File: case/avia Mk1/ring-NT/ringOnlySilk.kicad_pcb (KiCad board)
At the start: 2 copper layers, 44 x 43.6 mm, 1 part

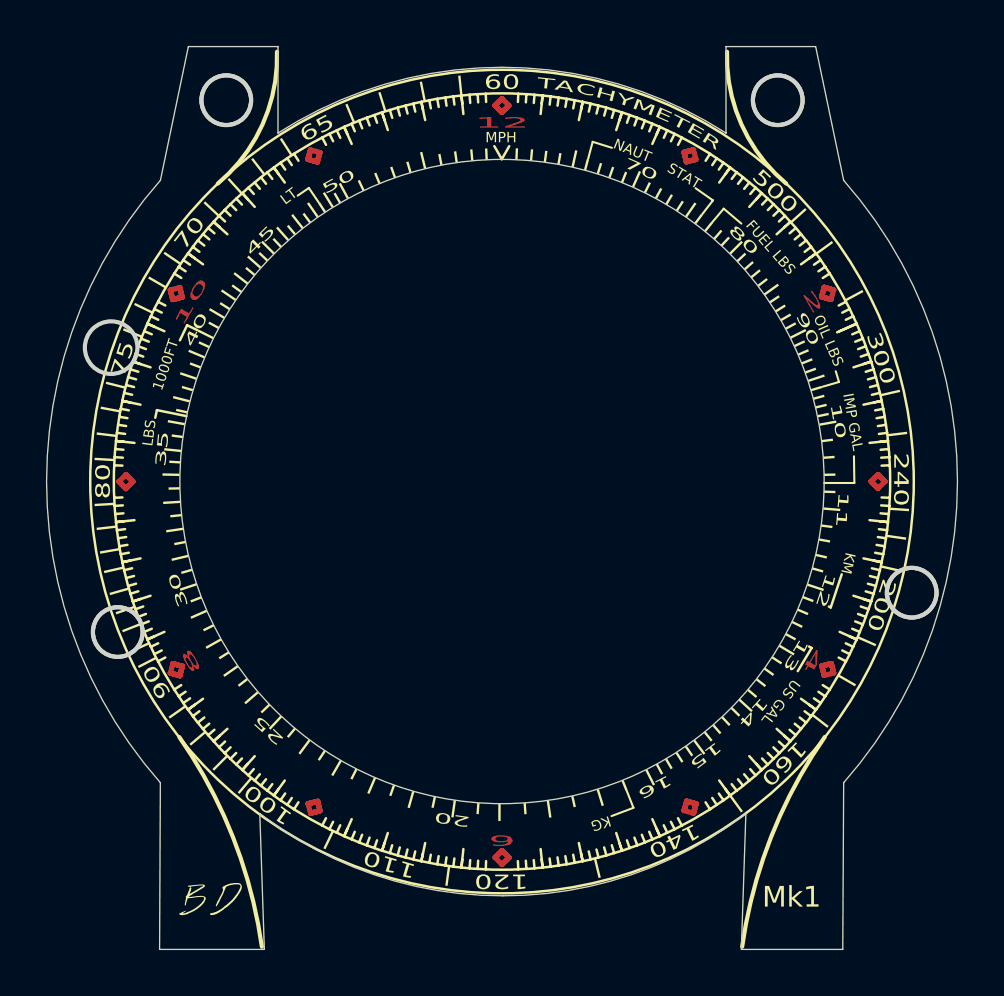
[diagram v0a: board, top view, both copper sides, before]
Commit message: no multiple definitions error
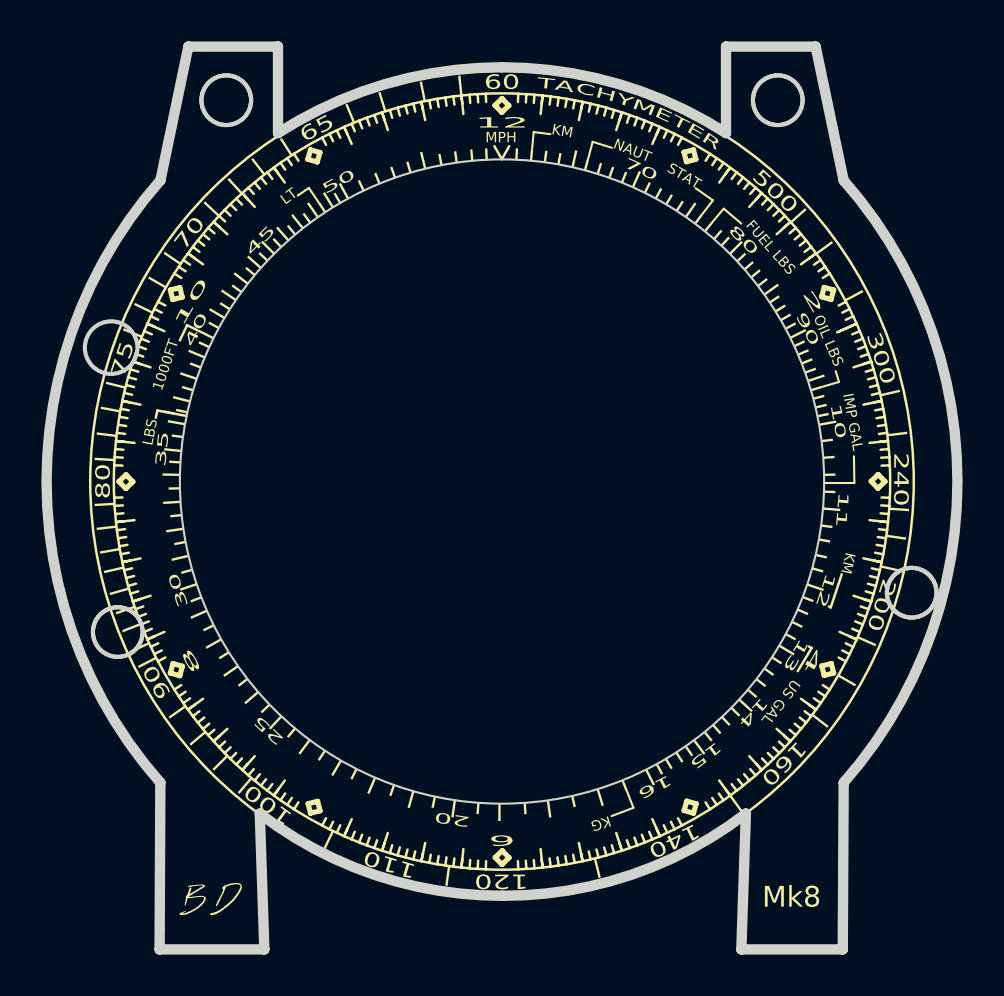
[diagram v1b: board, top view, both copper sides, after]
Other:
- board text added: "Mk8"
- board text added: "libra Mk8 navigator Watch cover"
- board text removed: "Mk1"
- board text removed: "avia ring v1.1"
